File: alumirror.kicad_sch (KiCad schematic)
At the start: 52 parts, among them SW1 SW_Push, SW10 SW_Push, SW11 SW_Push, SW12 SW_Push, SW13 SW_Push, SW14 SW_Push, SW15 SW_Push, SW16 SW_Push, SW17 SW_Push, SW18 SW_Push, SW19 SW_Push, SW2 SW_Push, SW20 SW_Push, SW3 SW_Push, SW4 SW_Push, SW5 SW_Push, SW6 SW_Push, SW7 SW_Push, SW8 SW_Push, SW9 SW_Push, U1 CH552T, U2 CH552T

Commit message: Add 3D model pocket areas for all matrix components
User 1–4 layers of switches, diodes and resistors now contain areas that will be excluded from the 3D print for the bottom-mid case. This will allow space for these components. These areas are constructed from shapes (e.g., the diode has two circles with a connecting rectangle) rather than lines. This is so that they can be imported straight into FreeCAD. Using arcs and lines would look cleaner, but the exported SVG files would need to be modified in design software to merge each group of lines into a single shape before import into FreeCAD.
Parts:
- R1, R10, R2, R3, R4, R5, R6, R7, R8, R9: footprint Resistor_SMD:R_2010_5025Metric -> Project Library:R_2010_5025Metric_Mod
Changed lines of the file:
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@@
 			)
 		)
-		(property "Footprint" "Resistor_SMD:R_2010_5025Metric"
+		(property "Footprint" "Project Library:R_2010_5025Metric_Mod"
 			(at 90.932 52.07 90)
 			(effects
@@
 			)
 		)
-		(property "Footprint" "Resistor_SMD:R_2010_5025Metric"
+		(property "Footprint" "Project Library:R_2010_5025Metric_Mod"
 			(at 167.132 57.15 90)
 			(effects
@@
 			)
 		)
-		(property "Footprint" "Resistor_SMD:R_2010_5025Metric"
+		(property "Footprint" "Project Library:R_2010_5025Metric_Mod"
 			(at 116.332 41.91 90)
 			(effects
@@
 			)
 		)
-		(property "Footprint" "Resistor_SMD:R_2010_5025Metric"
+		(property "Footprint" "Project Library:R_2010_5025Metric_Mod"
 			(at 116.332 62.23 90)
 			(effects
@@
 			)
 		)
-		(property "Footprint" "Resistor_SMD:R_2010_5025Metric"
+		(property "Footprint" "Project Library:R_2010_5025Metric_Mod"
 			(at 141.732 57.15 90)
 			(effects
@@
 			)
 		)
-		(property "Footprint" "Resistor_SMD:R_2010_5025Metric"
+		(property "Footprint" "Project Library:R_2010_5025Metric_Mod"
 			(at 217.932 52.07 90)
 			(effects
@@
 			)
 		)
-		(property "Footprint" "Resistor_SMD:R_2010_5025Metric"
+		(property "Footprint" "Project Library:R_2010_5025Metric_Mod"
 			(at 192.532 41.91 90)
 			(effects
@@
 			)
 		)
-		(property "Footprint" "Resistor_SMD:R_2010_5025Metric"
+		(property "Footprint" "Project Library:R_2010_5025Metric_Mod"
 			(at 192.532 62.23 90)
 			(effects
@@
 			)
 		)
-		(property "Footprint" "Resistor_SMD:R_2010_5025Metric"
+		(property "Footprint" "Project Library:R_2010_5025Metric_Mod"
 			(at 141.732 36.83 90)
 			(effects
@@
 			)
 		)
-		(property "Footprint" "Resistor_SMD:R_2010_5025Metric"
+		(property "Footprint" "Project Library:R_2010_5025Metric_Mod"
 			(at 167.132 36.83 90)
 			(effects

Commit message: Re-work thumb key connections
The lefthand thumb keys are now on row 2, columns 0 and 5. This frees up a pin for potential red, green *and blue* LEDs.

The righthand thumb keys remain on their own row. This is easier to route and allows for a 5-way navigation switch to be added.
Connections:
- net Col0: now also SW20.1
- net Col5L: now also SW19.1
- net Row2: now also D19.1 (K), D20.1 (K)
- net at R9.2, SW15.1: no longer SW19.1
- net at R10.2, SW16.1: no longer SW20.1
- net LED_G: now reaches U2.12 (P3.4)
- net LED_R: now reaches U2.13 (P3.5)
- removed net Row3L: D19.1 (K), D20.1 (K), U2.11 (P3.3)
- new net LED_B: U2.11 (P3.3)

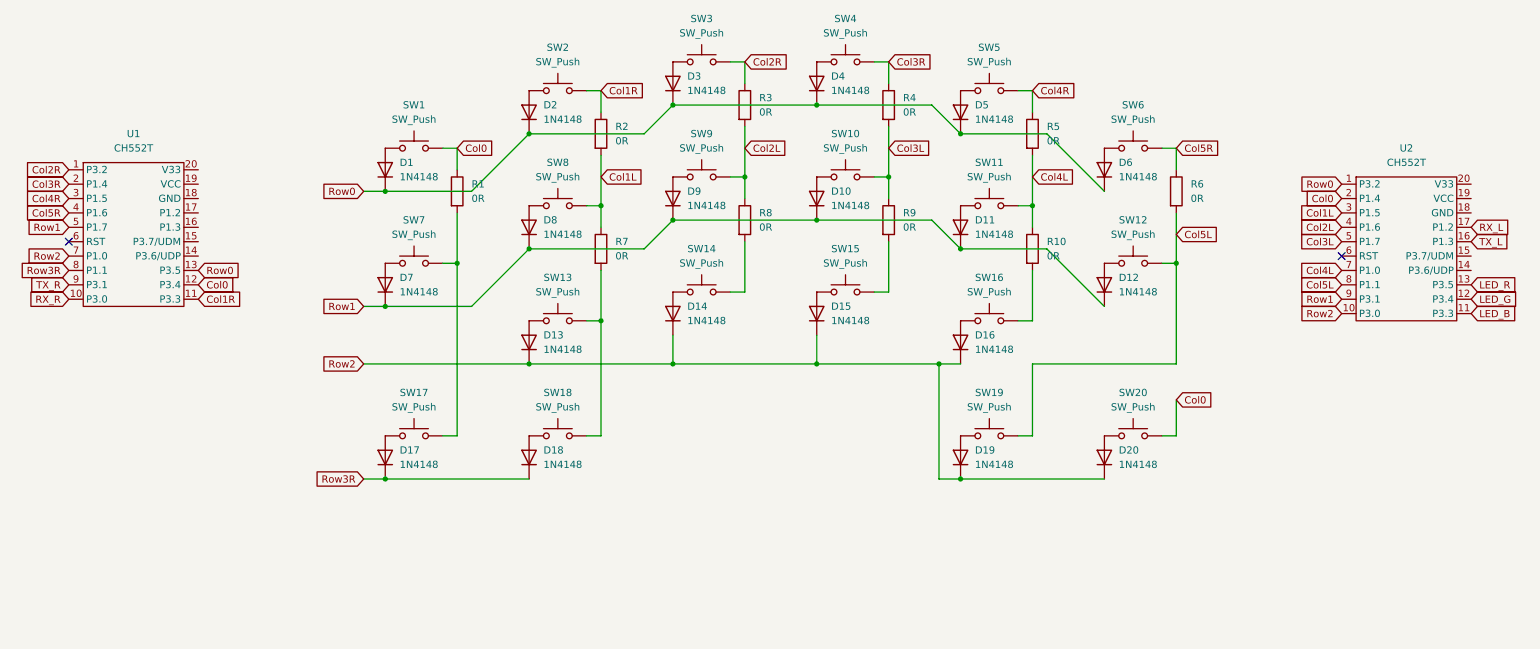
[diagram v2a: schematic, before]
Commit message: Add nav. switch proof-of-concept
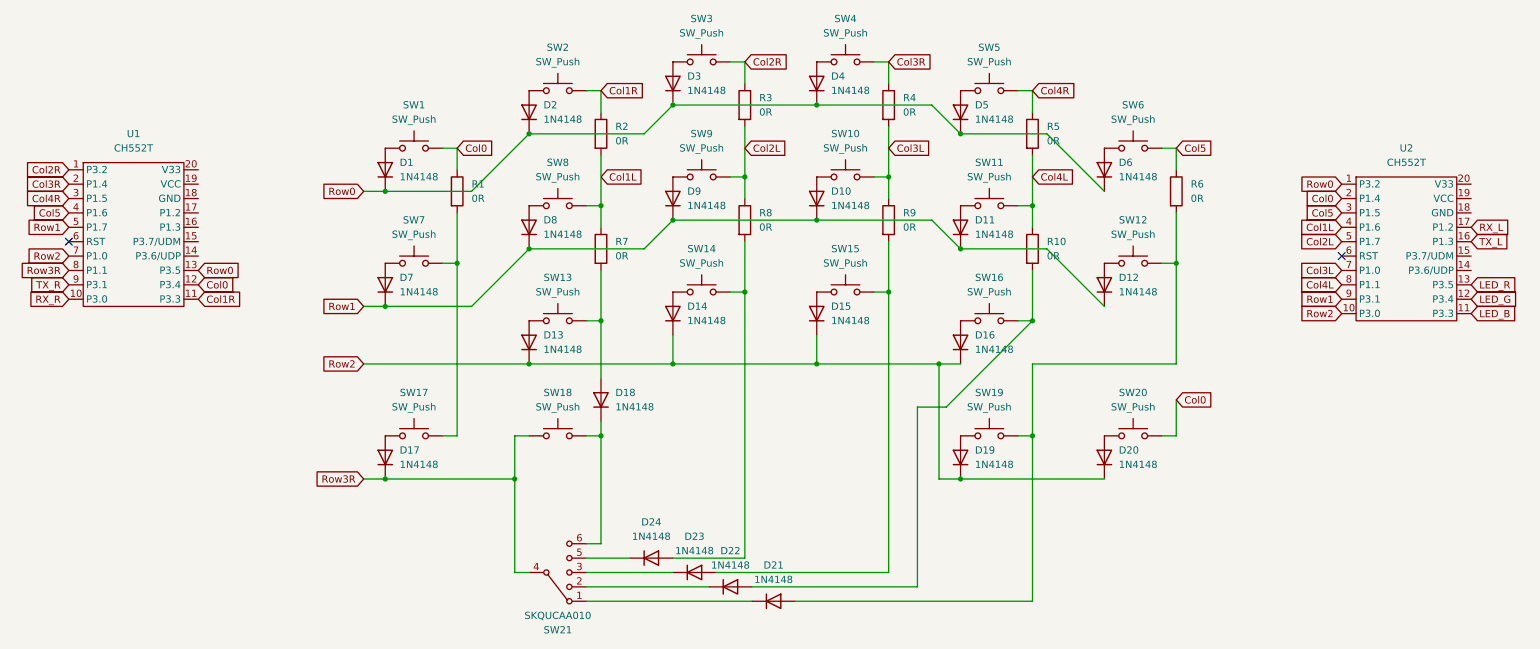
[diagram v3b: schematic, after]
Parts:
- added D21, D22, D23, D24: 1N4148, Project Library:D_SOD-123_Mod, symbol Device:D
- added SW21: SKQUCAA010, Project Library:Nav_Switch_SKQUAAA010, symbol Project Library:SW_SP5T
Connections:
- net Col1L: now also U2.4 (P1.6); no longer U2.3 (P1.5)
- net Col2L: now also U2.5 (P1.7); no longer U2.4 (P1.6)
- net Col3L: now also U2.7 (P1.0); no longer U2.5 (P1.7)
- net Col4L: now also U2.8 (P1.1); no longer U2.7 (P1.0)
- net Row3R: now also SW18.2, SW21.4 (Com); no longer D18.1 (K)
- net at R7.2, SW13.1: now also D18.2 (A); no longer SW18.1
- net at R9.2, SW15.1: now also D23.2 (A)
- net at R8.2, SW14.1: now also D24.2 (A)
- net at R10.2, SW16.1: now also D22.2 (A)
- net Col5L: no longer names the net of R6.2, SW12.1, SW19.1
- net Col5L: now also D21.2 (A); no longer U2.8 (P1.1)
- net Col5R renamed Col5
- net Col5: now also U2.3 (P1.5)
- new net: D23.1 (K), SW21.3 (C)
- new net: D18.1 (K), SW18.1, SW21.6 (Ctr)
- new net: D21.1 (K), SW21.1 (A)
- new net: D24.1 (K), SW21.5 (D)
- new net: D22.1 (K), SW21.2 (B)

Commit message: Renumber switches and diode by row and column
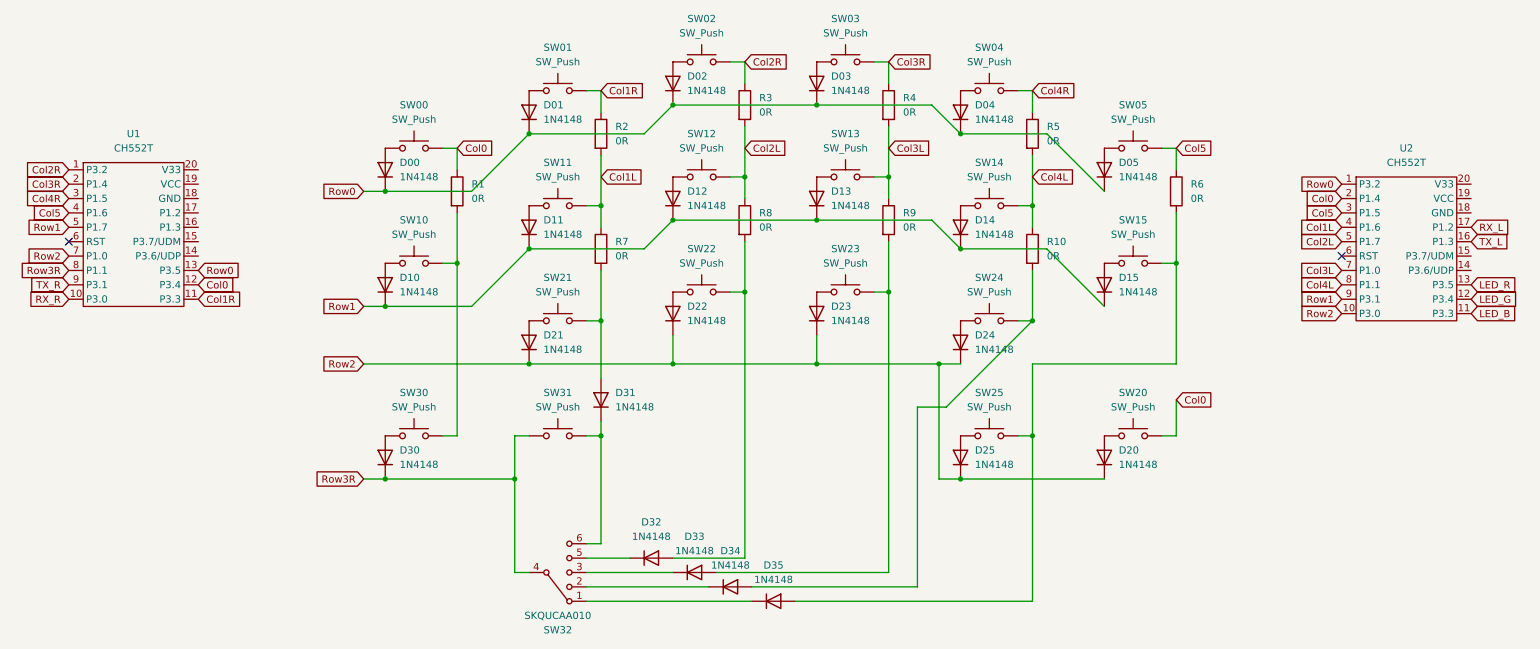
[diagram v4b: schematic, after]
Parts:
- renumbered D1 to D00, D2 to D01, D3 to D02, D4 to D03, D5 to D04, D6 to D05, D7 to D10, D8 to D11, D9 to D12, D10 to D13, D11 to D14, D12 to D15, D13 to D21, D14 to D22, D15 to D23, D16 to D24, D19 to D25, D17 to D30, D18 to D31, D24 to D32, D23 to D33, D22 to D34, D21 to D35, SW1 to SW00, SW2 to SW01, SW3 to SW02, SW4 to SW03, SW5 to SW04, SW6 to SW05, SW7 to SW10, SW8 to SW11, SW9 to SW12, SW10 to SW13, SW11 to SW14, SW12 to SW15, SW13 to SW21, SW14 to SW22, SW15 to SW23, SW16 to SW24, SW19 to SW25, SW17 to SW30, SW18 to SW31, SW21 to SW32

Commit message: Create combined choc/nav. switch footprint and use for SW31
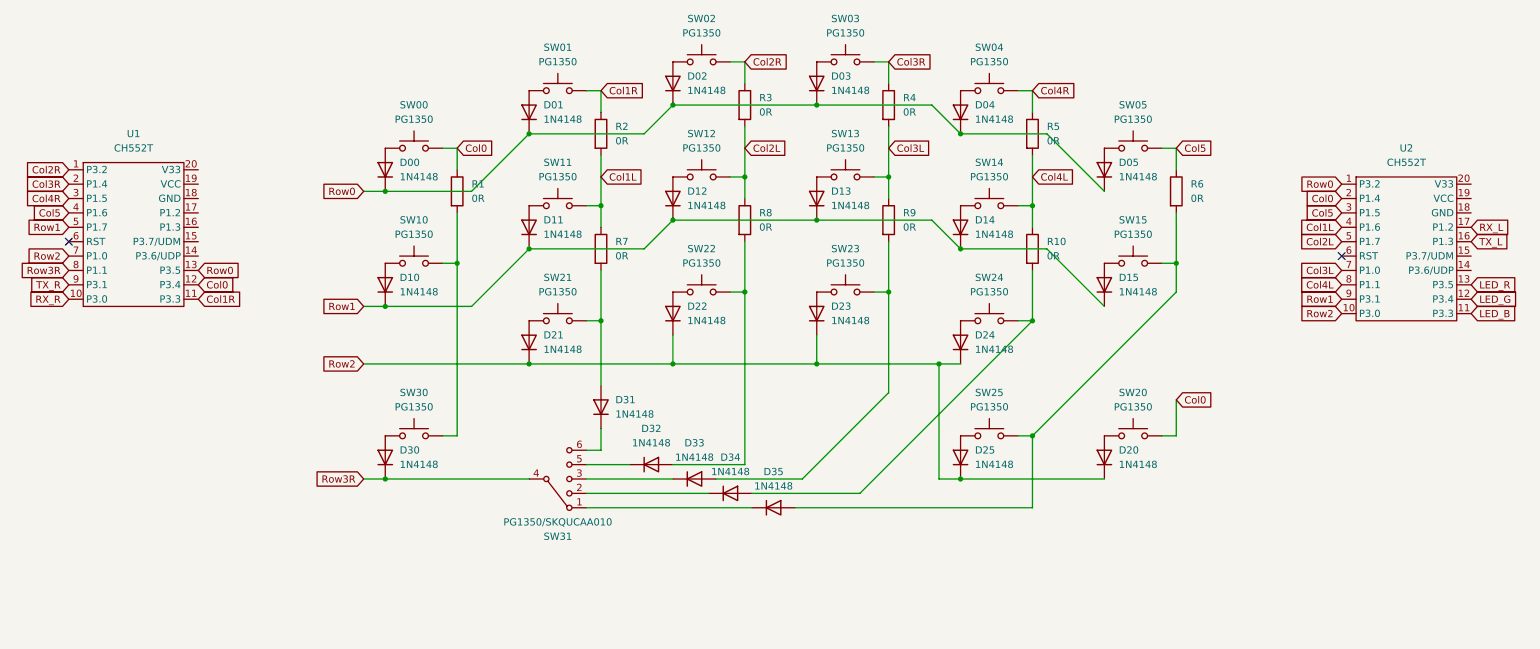
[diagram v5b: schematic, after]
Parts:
- removed SW31: SW_Push, Project Library:SW_choc_v1_HS_CPG135001S30_1layer_1u, symbol Switch:SW_Push
- SW00, SW01, SW02, SW03, SW04, SW05, SW10, SW11, SW12, SW13, SW14, SW15, SW20, SW21, SW22, SW23, SW24, SW25, SW30: value SW_Push -> PG1350
- SW31: renamed from SW32; value SKQUCAA010 -> PG1350/SKQUCAA010; footprint Project Library:Nav_Switch_SKQUAAA010 -> Project Library:SW_choc_v1_HS_nav_CPG135001S30_SKQUCAA010_1layer_1u_1
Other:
- moved on the sheet: D31, D32, D33, D34, D35, SW31

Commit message: Flop board
Switches now go in the correct column order (right to left when viewed from the copper side of the PCB) and the navigation switch is on the right thumb.
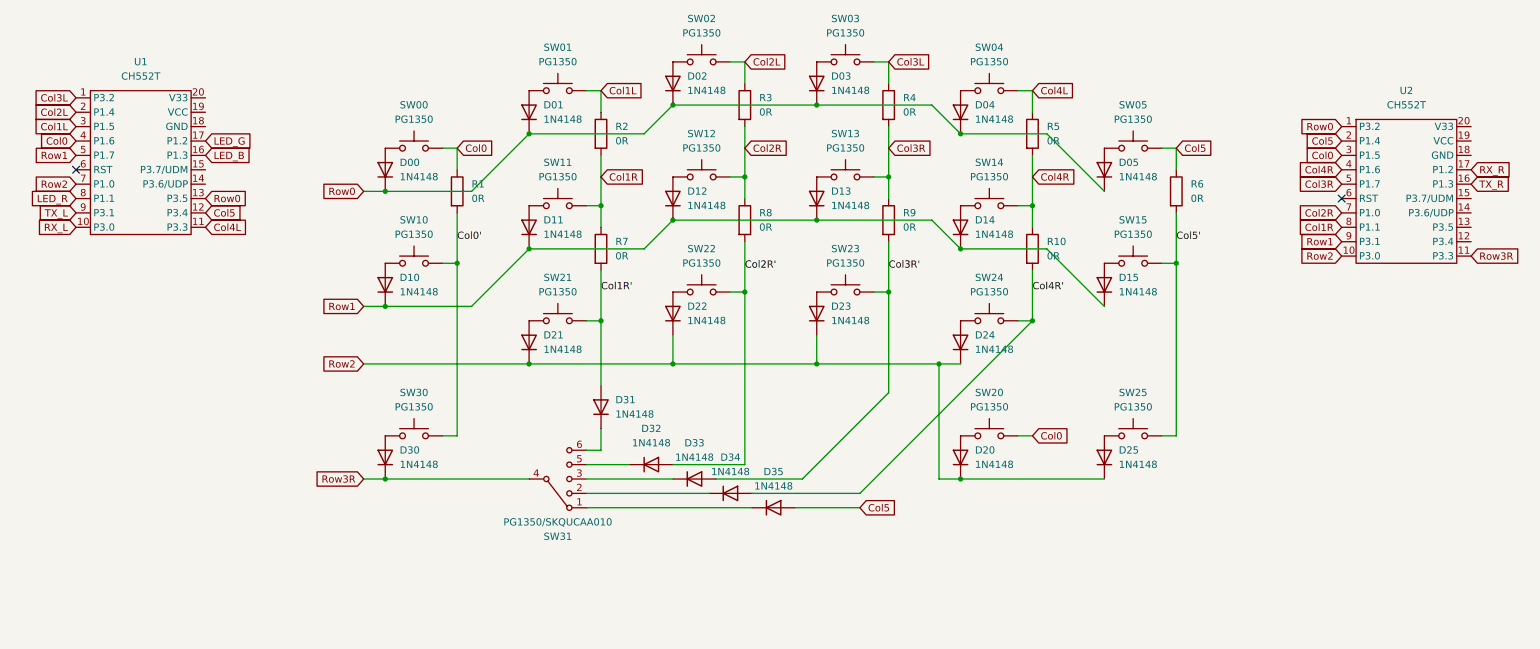
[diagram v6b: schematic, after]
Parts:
- renumbered D25 to D20, D20 to D25, SW25 to SW20, SW20 to SW25
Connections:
- net Col0: now also SW20.1, U1.4 (P1.6), U2.3 (P1.5); no longer SW25.1, U1.12 (P3.4), U2.2 (P1.4)
- net Col1L: now also R2.1, SW01.1, U1.3 (P1.5); no longer R2.2, R7.1, SW11.1, U2.4 (P1.6)
- net Col1R: now also R2.2, R7.1, SW11.1, U2.8 (P1.1); no longer R2.1, SW01.1, U1.11 (P3.3)
- net Col2L: now also R3.1, SW02.1, U1.2 (P1.4); no longer R3.2, R8.1, SW12.1, U2.5 (P1.7)
- net Col2R: now also R3.2, R8.1, SW12.1, U2.7 (P1.0); no longer R3.1, SW02.1, U1.1 (P3.2)
- net Col3L: now also R4.1, SW03.1, U1.1 (P3.2); no longer R4.2, R9.1, SW13.1, U2.7 (P1.0)
- net Col3R: now also R4.2, R9.1, SW13.1, U2.5 (P1.7); no longer R4.1, SW03.1, U1.2 (P1.4)
- net Col4L: now also R5.1, SW04.1, U1.11 (P3.3); no longer R10.1, R5.2, SW14.1, U2.8 (P1.1)
- net Col4R: now also R10.1, R5.2, SW14.1, U2.4 (P1.6); no longer R5.1, SW04.1, U1.3 (P1.5)
- net Col5: now also D35.2 (A), U1.12 (P3.4), U2.2 (P1.4); no longer U1.4 (P1.6), U2.3 (P1.5)
- net LED_B: now also U1.16 (P1.3); no longer U2.11 (P3.3)
- net LED_G: now also U1.17 (P1.2); no longer U2.12 (P3.4)
- net LED_R: now also U1.8 (P1.1); no longer U2.13 (P3.5)
- net RX_L: now also U1.10 (P3.0); no longer U2.17 (P1.2)
- net RX_R: now also U2.17 (P1.2); no longer U1.10 (P3.0)
- net Row3R: now also U2.11 (P3.3); no longer U1.8 (P1.1)
- net TX_L: now also U1.9 (P3.1); no longer U2.16 (P1.3)
- net TX_R: now also U2.16 (P1.3); no longer U1.9 (P3.1)
- net Col3R': now reaches D33.2 (A), R9.2, SW23.1
- net Col1R': now reaches D31.2 (A), R7.2, SW21.1
- net Col0': now reaches R1.2, SW10.1, SW30.1
- net Col5': now reaches R6.2, SW15.1
- net Col5': now also SW25.1; no longer D35.2 (A), SW20.1
- net Col2R': now reaches D32.2 (A), R8.2, SW22.1
- net Col4R': now reaches D34.2 (A), R10.2, SW24.1
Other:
- moved on the sheet: U1, U2

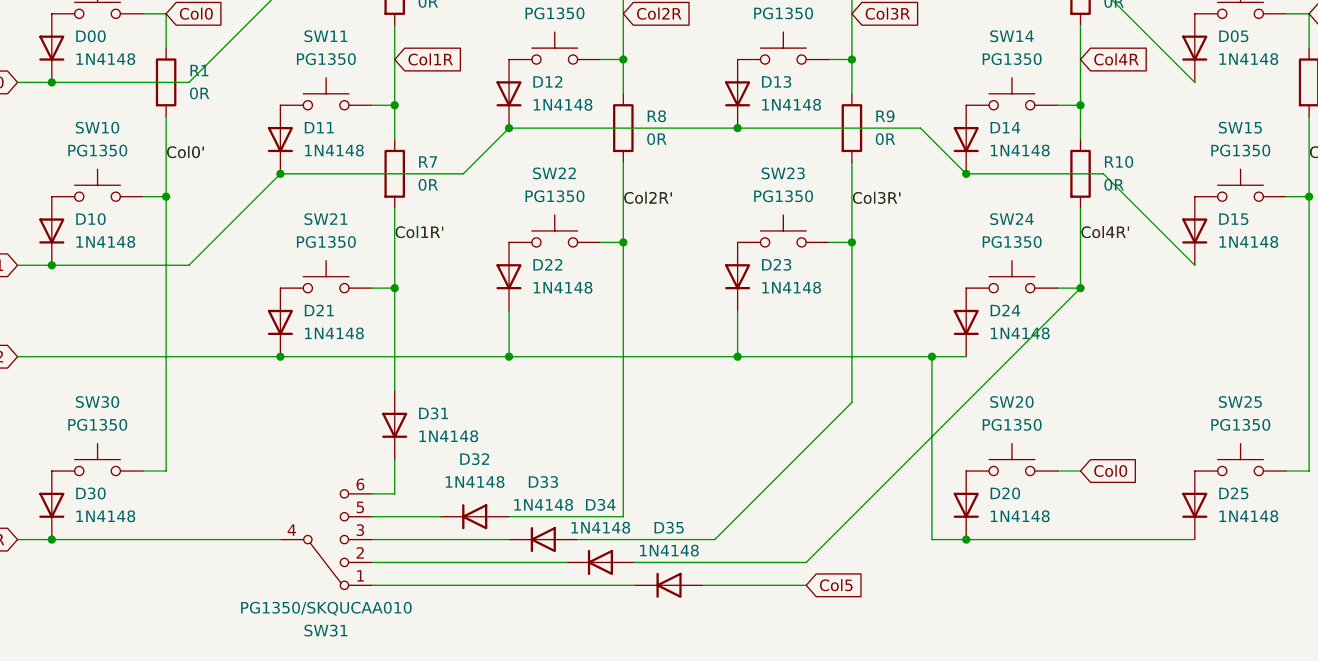
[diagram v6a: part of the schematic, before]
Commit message: Move bottom row one column over
This allows the left thumb keys to be on adjacent columns and saves routing Column 0 all the way across the board.
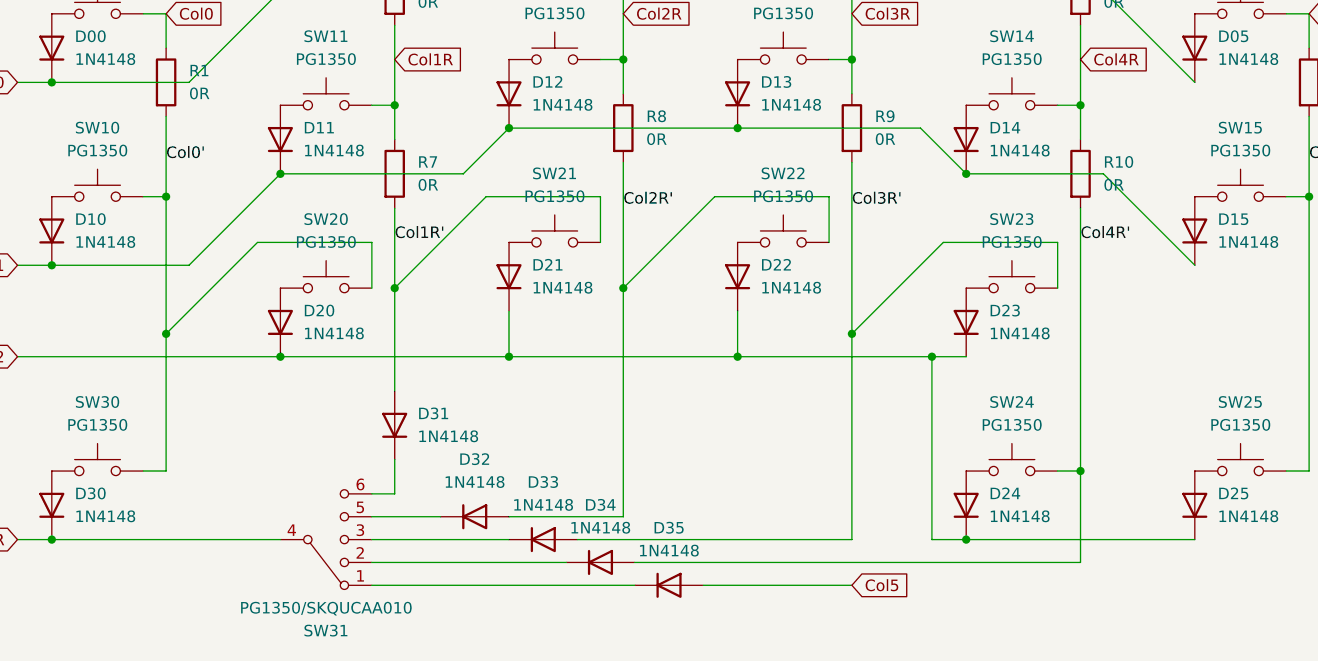
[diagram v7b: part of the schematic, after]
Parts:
- renumbered D21 to D20, D22 to D21, D23 to D22, D24 to D23, D20 to D24, SW21 to SW20, SW22 to SW21, SW23 to SW22, SW24 to SW23, SW20 to SW24
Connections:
- net Col0: no longer SW24.1
- net Col0': now also SW20.1
- net Col1R': now also SW21.1; no longer SW20.1
- net Col2R': now also SW22.1; no longer SW21.1
- net Col3R': now also SW23.1; no longer SW22.1
- net Col4R': now also SW24.1; no longer SW23.1

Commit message: Tidy schematic
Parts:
- SW25, SW30: value PG1350 -> PG1350_1½U
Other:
- moved on the sheet: D20, D21, D22, D23, D31, D32, D33, D34, D35, SW31
